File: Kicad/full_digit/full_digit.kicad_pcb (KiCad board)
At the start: 2 copper layers, 106.7 x 152.4 mm, 40 parts, among them J1 CONN_8, J2 CONN_8, J3 CONN_8, J4 CONN_8, J5 CONN_8, J6 CONN_8, J7 CONN_8, J8 CONN_8, U1 TLC5917, X1 MTHOLE, X2 MTHOLE, X3 MTHOLE, X4 MTHOLE

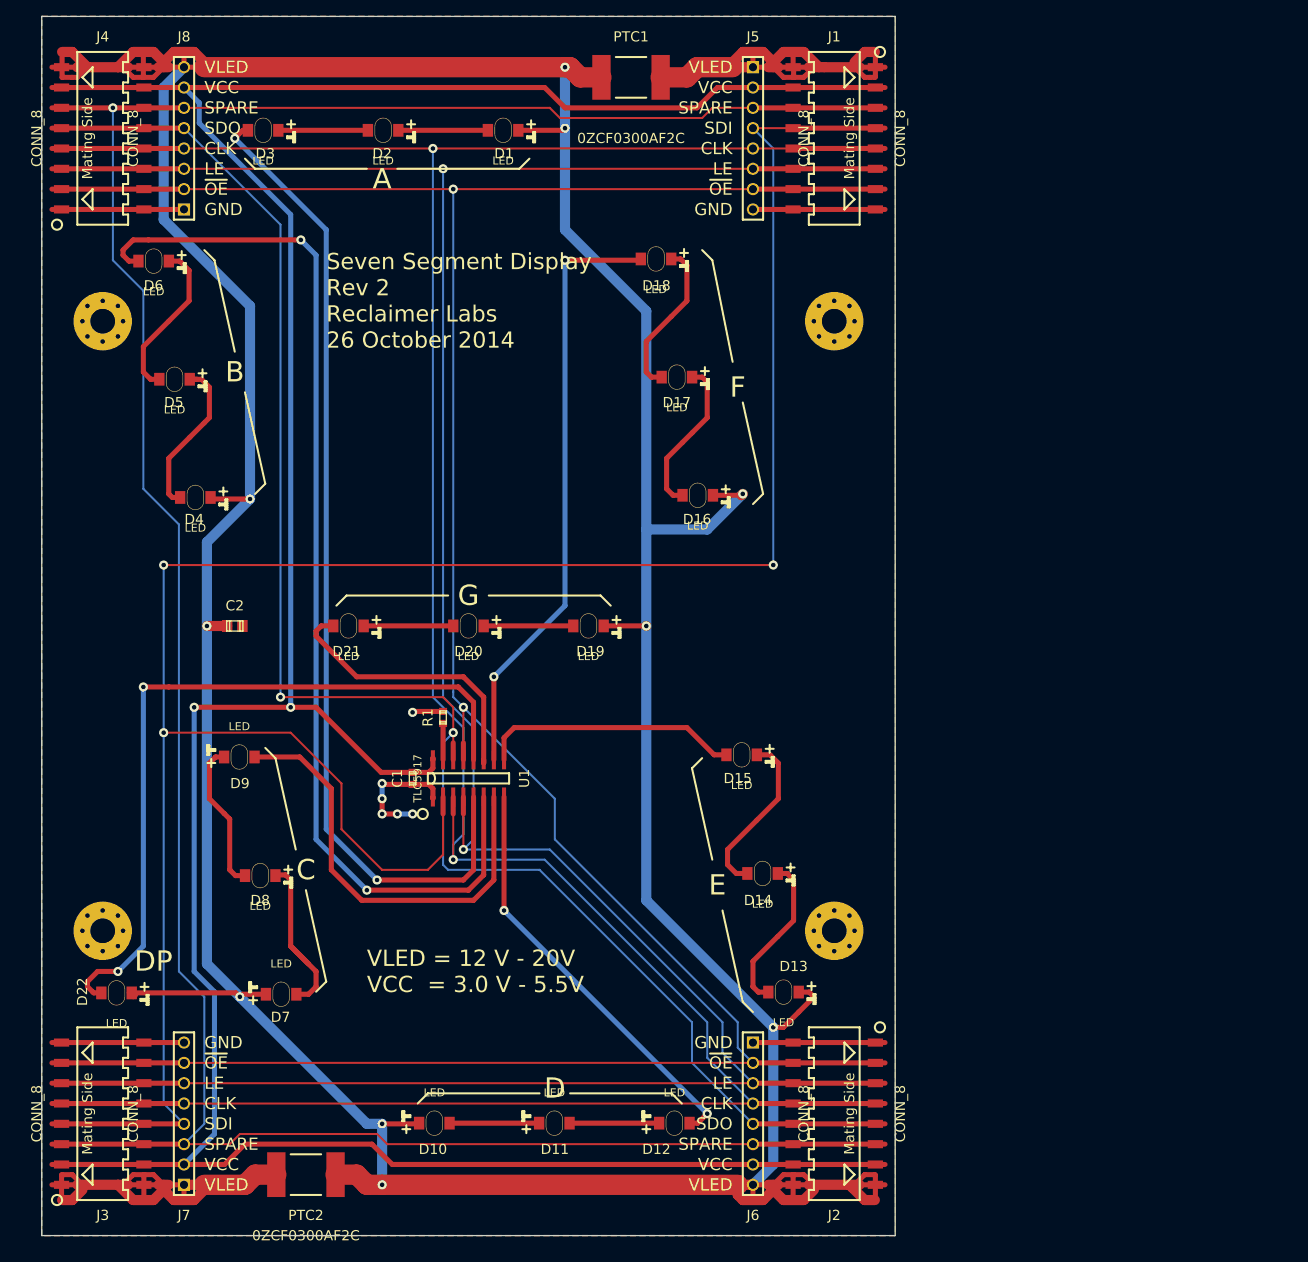
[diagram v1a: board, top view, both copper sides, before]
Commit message: Placement of Rev 3
Placed new parts: Spark, Arduino Uno, Arduino Micro, and logo. Routing
still to do.
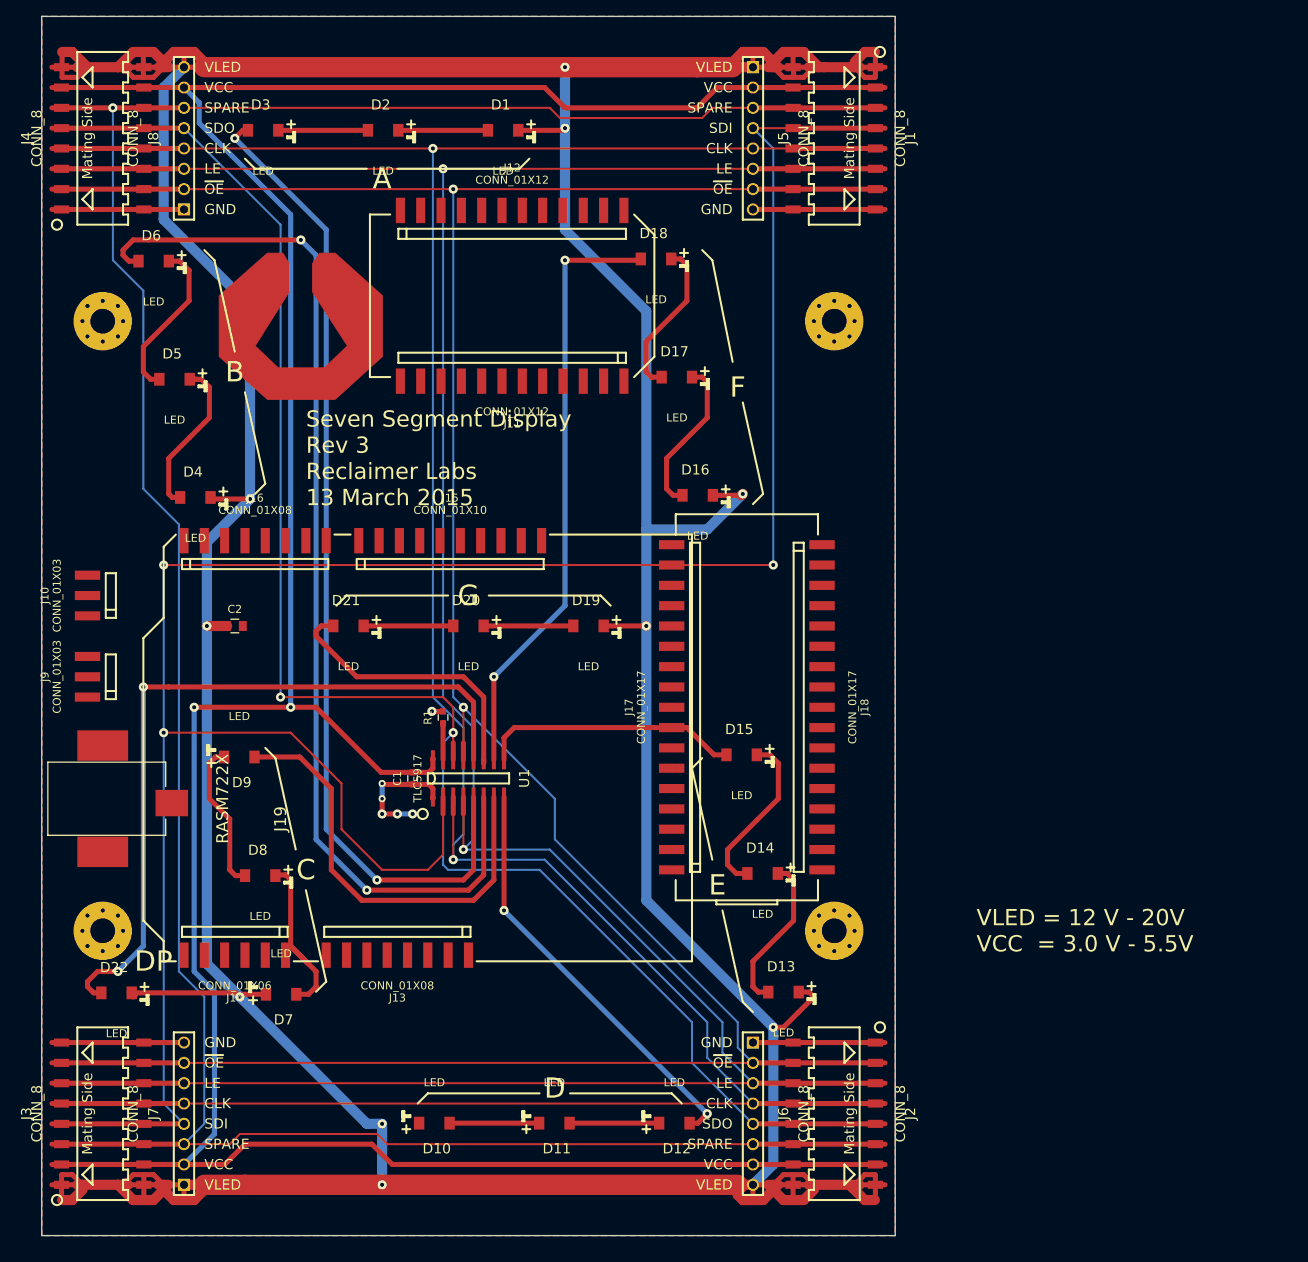
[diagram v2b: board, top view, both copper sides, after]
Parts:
- removed PTC1, PTC2: 0ZCF0300AF2C, 2920_ptc
- added G***: LOGO, Jason_Libraries:Reclaimer_Labs, F.Cu at (101.0, 107.3)
- added J10: CONN_01X03, Jason_Libraries:HEADER_SMT_01x03, F.Cu at (74.3, 141.0)
- added J11: CONN_01X12, Jason_Libraries:HEADER_SMT_01x12, F.Cu at (127.4, 114.2)
- added J12: CONN_01X12, Jason_Libraries:HEADER_SMT_01x12, F.Cu at (127.4, 92.8)
- added J13: CONN_01X08, Jason_Libraries:HEADER_SMT_01x08, F.Cu at (113.0, 185.9)
- added J14: CONN_01X06, Jason_Libraries:HEADER_SMT_01x06, F.Cu at (92.7, 185.9)
- added J15: CONN_01X10, Jason_Libraries:HEADER_SMT_01x10, F.Cu at (119.6, 134.1)
- added J16: CONN_01X08, Jason_Libraries:HEADER_SMT_01x08, F.Cu at (95.2, 134.1)
- added J17: CONN_01X17, Jason_Libraries:HEADER_SMT_01x17, F.Cu at (147.3, 154.9)
- added J18: CONN_01X17, Jason_Libraries:HEADER_SMT_01x17, F.Cu at (166.1, 154.9)
- added J19: RASM722X, Jason_Libraries:RASM722, F.Cu at (76.2, 166.4)
- added J9: CONN_01X03, Jason_Libraries:HEADER_SMT_01x03, F.Cu at (74.3, 151.1)
- C1, R1: footprint c_0603 -> Capacitors_SMD:C_0603
- C2: value 4.7uF 25V -> 4.7uF 50V; footprint c_0805 -> Capacitors_SMD:C_0805
- D1, D10, D11, D12, D13, D14, D15, D16, D17, D18, D19, D2, D20, D21, D22, D3, D4, D5, D6, D7, D8, D9: footprint 1206_LED_Reverse -> Jason_Libraries:1206_LED_Reverse
- J1, J2, J3, J4: footprint SSM-SH-08 -> Jason_Libraries:SSM-SH-08
- J5, J6, J7, J8: footprint HEADER_8X1 -> Jason_Libraries:HEADER_8X1
- U1: footprint SOIC16_Jason -> Jason_Libraries:SOIC16_Jason
- X1, X2, X3, X4: footprint MTHOLE_3mm -> Jason_Libraries:MTHOLE_3mm
- turned C1 to 270 degrees
- turned C2 to 0 degrees
- turned R1 to 90 degrees
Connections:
- J1 pad 1: N-0000020 -> Vled
- J3 pad 1: N-0000034 -> Vled
- J5 pad 1: N-0000020 -> Vled
- J7 pad 1: N-0000034 -> Vled
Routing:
- net Vled: track 588.7 -> 726.4 mm
- net N-0000034: track 65.0 -> 0.00 mm
- net N-0000020: track 64.6 -> 0.00 mm
- net GND: track 258.2 -> 255.7 mm
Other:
- net class Default: via_drill 0.635 -> 0.508
- net class LED: via_drill 0.635 -> 0.508
- net class Power: via_drill 0.635 -> 0.508
- net class SuperWide: via_drill 0.635 -> 0.508
- rule via_min_size: 0.889 -> 1.143
- board text added: "Seven Segment Display Rev 3 Reclaimer Labs 13 March 2015"
- board text removed: "Seven Segment Display Rev 2 Reclaimer Labs 26 October 2014"

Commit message: Rev 3 Final Draft
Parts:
- added G***: LOGO, Jason_Libraries:OSHW_Logo, F.Cu at (104.8, 118.1)
- J11, J12: footprint Jason_Libraries:HEADER_SMT_01x12 -> Jason_Libraries:HEADER_SMT_01x12_SV
- moved J12 79.1 mm to (127.9, 172.0), turned to 180 degrees
- moved C1 44.6 mm to (118.1, 119.4)
- moved U1 44.6 mm to (125.1, 119.4)
- moved R1 44.6 mm to (121.9, 111.8)
- moved J18 42.7 mm to (123.8, 160.9), turned to 0 degrees
- moved J11 36.5 mm to (127.9, 150.6), turned to 0 degrees
- moved J17 34.1 mm to (123.8, 179.7), turned to 180 degrees
- moved G*** 9.09 mm to (104.8, 99.1)
- moved C2 8.35 mm to (84.5, 146.1)
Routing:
- net VCC: track 390.2 -> 679.1 mm, vias 2 -> 7
- net /LE: track 352.6 -> 570.4 mm, vias 2 -> 7
- net /CLK: track 359.8 -> 508.9 mm, vias 2 -> 4
- net Vled: track 726.4 -> 872.7 mm, vias 10 -> 15
- net GND: track 255.7 -> 393.1 mm, vias 38 -> 57
- net /SPARE: track 345.7 -> 452.0 mm, vias 1 -> 4
- net /~OE: track 339.6 -> 432.0 mm, vias 2 -> 6
- net +5V: track 0.00 -> 82.5 mm
- net /SDO: track 210.0 -> 287.3 mm, vias 2 -> 3
- net Net-(D6-Pad2): track 135.5 -> 83.9 mm, vias 2 -> 0
- net Net-(D12-Pad2): track 52.8 -> 101.2 mm
- net Net-(D22-Pad2): track 93.6 -> 136.7 mm
- net Net-(D3-Pad2): track 123.8 -> 81.7 mm
- net Net-(D18-Pad2): track 75.7 -> 36.7 mm
- net Net-(D21-Pad2): track 35.8 -> 70.3 mm, vias 0 -> 2
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- added copper zone on F.Cu, net Vled
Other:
- rule via_min_size: 1.143 -> 1.016
- board text added: "+5V"
- board text added: "1. All requests for design or material changes must be forwarded to Jason Cerundolo. No design or material changes shall be implemented without approval from Jason Cerundolo (jason@reclaimerlabs.com)."
- board text added: "12-20VDC"
- board text added: "5. FABRICATION TOLERANCES: Trace/Space 10/10 mils. Trace width must maintain a +/- 20% in tolerance. All holes and registration must be within 0.010 inch of true position."
- board text added: "=3.0-5.5 VDC"
- board text added: "Arduino Micro"
- board text added: "Arduino Uno"
- board text added: "Arduino/Sparkfun Pro Micro"
- board text added: "Seven Segment Display Rev 3 Reclaimer Labs http://reclaimerlabs.com 22 March 2015"
- board text added: "Spark"
- board text removed: "1. All requests for design or material changes must be forwarded to Jason Cerundolo. No design or material changes shall be implemented without approval from Jason Cerundolo (jason@cerundolo.com)."
- board text removed: "5. FABRICATION TOLERANCES: Trace/Space 8/8 mils. Trace width must maintain a +/- 20% in tolerance. All holes and registration must be within 0.008 inch of true position."
- board text removed: "Seven Segment Display Rev 3 Reclaimer Labs 13 March 2015"
- board text removed: "VLED = 12 V - 20V VCC = 3.0 V - 5.5V"
